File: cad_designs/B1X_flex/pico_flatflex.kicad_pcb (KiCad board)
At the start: 2 copper layers, 69.8 x 28.7 mm, 17 parts, among them J32 Conn_01x01, U1 Pico

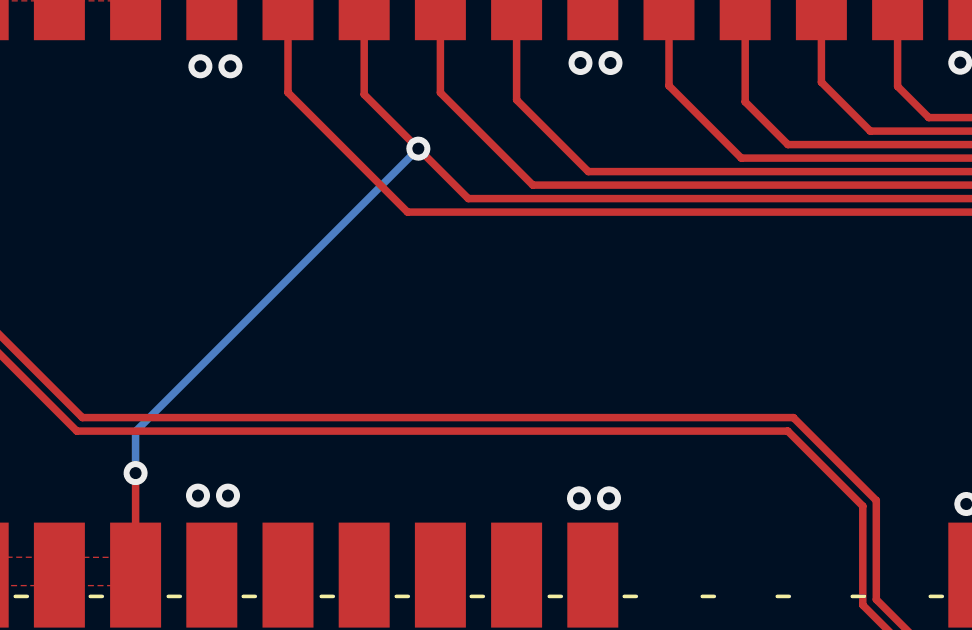
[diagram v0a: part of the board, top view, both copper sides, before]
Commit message: Add credits and WUP-50 warning
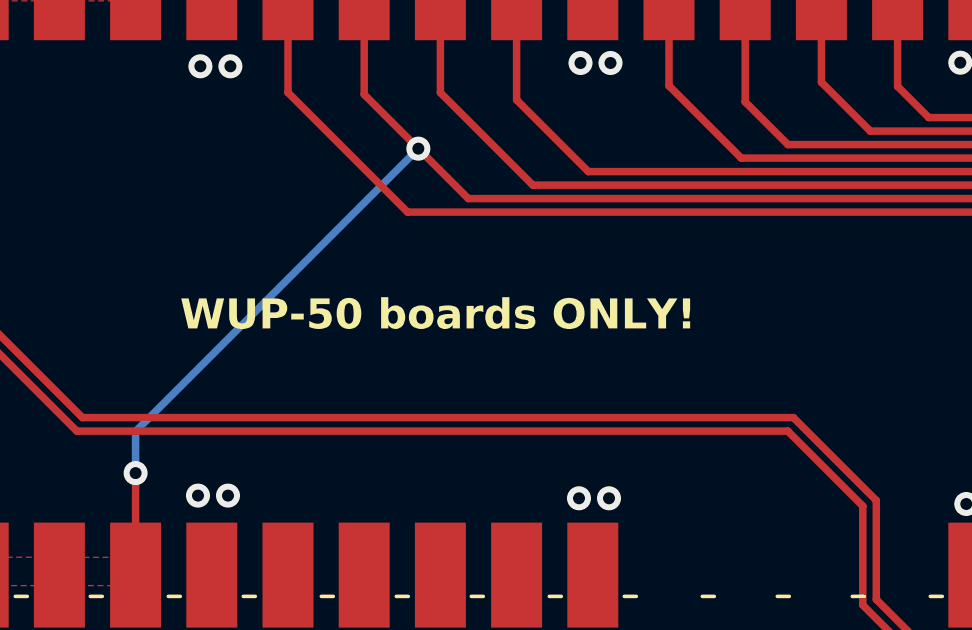
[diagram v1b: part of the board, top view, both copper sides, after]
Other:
- board text added: "Flex by Lazr1026 de_Fuse by Shinyquagsire23"
- board text added: "WUP-50 boards ONLY!"
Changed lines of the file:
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@@
 				(color "Polyimide")
 				(thickness 0.03)
+				(material "FR4")
+				(epsilon_r 4.5)
+				(loss_tangent 0.02)
 			)
 			(layer "B.Cu"
@@
 		(layer "Edge.Cuts")
 	)
+	(gr_text "Flex by Lazr1026\nde_Fuse by Shinyquagsire23\n"
+		(at 142.2 66.75 0)
+		(layer "B.SilkS")
+		(effects
+			(font
+				(size 1 1)
+				(thickness 0.3)
+				(bold yes)
+			)
+			(justify left bottom mirror)
+		)
+	)
+	(gr_text "WUP-50 boards ONLY!"
+		(at 110.12 76.61 0)
+		(layer "F.SilkS")
+		(effects
+			(font
+				(size 1 1)
+				(thickness 0.25)
+				(bold yes)
+			)
+			(justify left bottom)
+		)
+	)
 	(segment
